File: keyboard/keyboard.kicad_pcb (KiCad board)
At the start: 4 copper layers, 83.3 x 34.3 mm, 23 parts, among them J1 Mini-DIN-6, J2 Conn_01x13, U1 74HC595, U2 74HC595, U3 74HC180, U4 74HC08, U5 74HC14

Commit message: Update keyboard
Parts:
- added C8: 1uF, Capacitor_THT:CP_Radial_D4.0mm_P2.00mm, F.Cu at (98.3, 62.9)
- H1, H2, H3, H4: footprint MountingHole:MountingHole_2.7mm_M2.5_Pad -> MountingHole:MountingHole_3.2mm_M3_Pad
- moved C2 2.29 mm to (89.9, 78.0)
- moved R3 1.93 mm to (90.1, 63.2)
- moved R2 1.80 mm to (89.9, 82.8)
- moved J1 1.50 mm to (82.3, 77.0), turned to 270 degrees
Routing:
- net VCC: track 146.6 -> 142.2 mm
- net KBD_DATA: track 28.9 -> 24.6 mm
- net KBD_CLK: track 87.1 -> 87.8 mm

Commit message: Update keyboard
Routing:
- added copper zone on F.Cu, net GND
- added copper zone on In1.Cu, net GND
- added copper zone on In2.Cu, net GND
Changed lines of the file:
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@@
     (pcbplotparams
       (layerselection 0x010fc_ffffffff)
-      (usegerberextensions false)
-      (usegerberattributes true)
-      (usegerberadvancedattributes true)
-      (creategerberjobfile true)
+      (usegerberextensions true)
+      (usegerberattributes false)
+      (usegerberadvancedattributes false)
+      (creategerberjobfile false)
       (excludeedgelayer true)
       (linewidth 0.100000)
@@
       (psa4output false)
       (plotreference true)
-      (plotvalue true)
+      (plotvalue false)
       (plotinvisibletext false)
       (padsonsilk false)
-      (subtractmaskfromsilk false)
+      (subtractmaskfromsilk true)
       (outputformat 1)
       (mirror false)
-      (drillshape 1)
+      (drillshape 0)
       (scaleselection 1)
-      (outputdirectory ""))
+      (outputdirectory "./gerbers"))
   )
   (net 0 "")
@@
       (effects (font (size 1 1) (thickness 0.15)))
     )
-    (fp_text user %R (at 0.3 0) (layer F.Fab)
-      (effects (font (size 1 1) (thickness 0.15)))
-    )
     (fp_circle (center 0 0) (end 3.2 0) (layer Cmts.User) (width 0.15))
     (fp_circle (center 0 0) (end 3.45 0) (layer F.CrtYd) (width 0.05))
+    (fp_text user %R (at 0.3 0) (layer F.Fab)
+      (effects (font (size 1 1) (thickness 0.15)))
+    )
     (pad 1 thru_hole circle (at 0 0) (size 6.4 6.4) (drill 3.2) (layers *.Cu *.Mask)
       (net 1 GND))
@@
       (effects (font (size 1 1) (thickness 0.15)))
     )
-    (fp_text user %R (at 0.3 0) (layer F.Fab)
-      (effects (font (size 1 1) (thickness 0.15)))
-    )
     (fp_circle (center 0 0) (end 3.2 0) (layer Cmts.User) (width 0.15))
     (fp_circle (center 0 0) (end 3.45 0) (layer F.CrtYd) (width 0.05))
+    (fp_text user %R (at 0.3 0) (layer F.Fab)
+      (effects (font (size 1 1) (thickness 0.15)))
+    )
     (pad 1 thru_hole circle (at 0 0) (size 6.4 6.4) (drill 3.2) (layers *.Cu *.Mask)
       (net 1 GND))
@@
       (effects (font (size 1 1) (thickness 0.15)))
     )
-    (fp_text user %R (at 0.3 0) (layer F.Fab)
-      (effects (font (size 1 1) (thickness 0.15)))
-    )
     (fp_circle (center 0 0) (end 3.2 0) (layer Cmts.User) (width 0.15))
     (fp_circle (center 0 0) (end 3.45 0) (layer F.CrtYd) (width 0.05))
+    (fp_text user %R (at 0.3 0) (layer F.Fab)
+      (effects (font (size 1 1) (thickness 0.15)))
+    )
     (pad 1 thru_hole circle (at 0 0) (size 6.4 6.4) (drill 3.2) (layers *.Cu *.Mask)
       (net 1 GND))
@@
       (effects (font (size 1 1) (thickness 0.15)))
     )
-    (fp_text user %R (at 0.3 0) (layer F.Fab)
-      (effects (font (size 1 1) (thickness 0.15)))
-    )
     (fp_circle (center 0 0) (end 3.2 0) (layer Cmts.User) (width 0.15))
     (fp_circle (center 0 0) (end 3.45 0) (layer F.CrtYd) (width 0.05))
+    (fp_text user %R (at 0.3 0) (layer F.Fab)
+      (effects (font (size 1 1) (thickness 0.15)))
+    )
     (pad 1 thru_hole circle (at 0 0) (size 6.4 6.4) (drill 3.2) (layers *.Cu *.Mask)
       (net 1 GND))
@@
       )
     )
+  )
+  (zone (net 1) (net_name GND) (layer F.Cu) (hatch edge 0.508)
+    (connect_pads (clearance 0.508))
+    (min_thickness 0.254)
+    (fill yes (arc_segments 32) (thermal_gap 0.508) (thermal_bridge_width 0.508))
+    (polygon
+      (pts
+        (xy 161.036 97.536) (xy 73.533 97.028) (xy 73.152 57.404) (xy 161.036 57.15)
+      )
+    )
+  )
+  (zone (net 1) (net_name GND) (layer In1.Cu) (hatch edge 0.508)
+    (connect_pads (clearance 0.508))
+    (min_thickness 0.254)
+    (fill yes (arc_segments 32) (thermal_gap 0.508) (thermal_bridge_width 0.508))
+    (polygon
+      (pts
+        (xy 161.29 97.536) (xy 73.406 96.901) (xy 73.406 57.531) (xy 161.29 57.15)
+      )
+    )
+  )
+  (zone (net 1) (net_name GND) (layer In2.Cu) (hatch edge 0.508)
+    (connect_pads (clearance 0.508))
+    (min_thickness 0.254)
+    (fill yes (arc_segments 32) (thermal_gap 0.508) (thermal_bridge_width 0.508))
+    (polygon
+      (pts
+        (xy 161.163 57.531) (xy 161.29 97.536) (xy 73.406 97.028) (xy 73.406 57.404)
+      )
+    )

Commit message: Update keyboard PCB
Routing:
- net KBD_CLK: track 87.8 -> 80.4 mm
- net VCC: track 142.2 -> 143.1 mm
- net KBD_DATA: track 24.6 -> 23.9 mm
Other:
- board text added: "PS/2 interface v1.1 Adrien Kohlbecker 2021-05-18"
- board text removed: "PS/2 interface v01 Adrien Kohlbecker 2021-05-18"
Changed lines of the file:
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@@
     (thickness 1.6)
     (drawings 27)
-    (tracks 261)
+    (tracks 260)
     (zones 0)
     (modules 24)
@@
     (add_net ~REG_CLK)
     (add_net ~REG_OE)
+  )
+  (module AK's_Footprints:Mini_din6 (layer F.Cu)
+    (at 82.2706 76.962 270)
+    (tags "MINI DIN")
+    (fp_text reference J1 (at 0 -7.62 270) (layer F.Fab)
+      (effects (font (size 1.524 1.524) (thickness 0.3048)))
+    )
+    (fp_text value Mini-DIN-6 (at 0 -10.16 90) (layer F.Fab)
+      (effects (font (size 1.524 1.524) (thickness 0.3048)))
+    )
+    (fp_line (start -6.35 1.27) (end -6.35 -5.68) (layer F.SilkS) (width 0.1))
+    (fp_line (start -6.35 -5.68) (end 6.35 -5.68) (layer F.SilkS) (width 0.1))
+    (fp_line (start 6.35 -5.68) (end 6.35 6.58) (layer F.SilkS) (width 0.1))
+    (fp_line (start 6.35 6.58) (end -6.35 6.58) (layer F.SilkS) (width 0.1))
+    (fp_line (start -6.35 6.58) (end -6.35 1.27) (layer F.SilkS) (width 0.1))
+    (pad GND thru_hole rect (at -6.985 1.27 270) (size 2.16916 3.2004) (drill oval 0.5 1.9) (layers *.Cu *.Mask)
+      (net 1 GND))
+    (pad GND thru_hole rect (at 6.985 1.27 270) (size 2.16916 3.2004) (drill oval 0.5 1.9) (layers *.Cu *.Mask)
+      (net 1 GND))
+    (pad GND thru_hole rect (at 0 1.8542 270) (size 3.2004 1.99898) (drill oval 1.9 0.5) (layers *.Cu *.Mask)
+      (net 1 GND))
+    (pad 3 thru_hole circle (at 3.175 -1.27 270) (size 1.7 1.7) (drill 0.75) (layers *.Cu *.Mask)
+      (net 1 GND))
+    (pad 4 thru_hole circle (at -3.175 -1.27 270) (size 1.7 1.7) (drill 0.75) (layers *.Cu *.Mask)
+      (net 3 VCC))
+    (pad 6 thru_hole circle (at -3.175 -3.81 270) (size 1.7 1.7) (drill 0.75) (layers *.Cu *.Mask))
+    (pad 5 thru_hole circle (at 3.175 -3.81 270) (size 1.7 1.7) (drill 0.75) (layers *.Cu *.Mask)
+      (net 16 KBD_CLK))
+    (pad 1 thru_hole circle (at 1.143 -1.27 270) (size 1.7 1.7) (drill 0.75) (layers *.Cu *.Mask)
+      (net 17 KBD_DATA))
+    (pad 2 thru_hole circle (at -1.016 -1.27 270) (size 1.7 1.7) (drill 0.75) (layers *.Cu *.Mask))
+    (model ":AKs Footprints:Mini_din6.wrl"
+      (at (xyz 0 0 0))
+      (scale (xyz 1 1 1))
+      (rotate (xyz 0 0 0))
+    )
   )
   (module MountingHole:MountingHole_3.2mm_M3_Pad (layer F.Cu)
@@
     )
   )
-  (module AK's_Footprints:Mini_din6 (layer F.Cu)
-    (at 82.2706 76.962 270)
-    (tags "MINI DIN")
-    (fp_text reference J1 (at 0 -7.62 270) (layer F.Fab)
-      (effects (font (size 1.524 1.524) (thickness 0.3048)))
-    )
-    (fp_text value Mini-DIN-6 (at 0 -10.16 90) (layer F.Fab)
-      (effects (font (size 1.524 1.524) (thickness 0.3048)))
-    )
-    (fp_line (start -6.35 1.27) (end -6.35 -5.68) (layer F.SilkS) (width 0.1))
-    (fp_line (start -6.35 -5.68) (end 6.35 -5.68) (layer F.SilkS) (width 0.1))
-    (fp_line (start 6.35 -5.68) (end 6.35 6.58) (layer F.SilkS) (width 0.1))
-    (fp_line (start 6.35 6.58) (end -6.35 6.58) (layer F.SilkS) (width 0.1))
-    (fp_line (start -6.35 6.58) (end -6.35 1.27) (layer F.SilkS) (width 0.1))
-    (pad GND thru_hole rect (at -6.985 1.27 270) (size 2.16916 3.2004) (drill oval 0.5 1.9) (layers *.Cu *.Mask)
-      (net 1 GND))
-    (pad GND thru_hole rect (at 6.985 1.27 270) (size 2.16916 3.2004) (drill oval 0.5 1.9) (layers *.Cu *.Mask)
-      (net 1 GND))
-    (pad GND thru_hole rect (at 0 1.8542 270) (size 3.2004 1.99898) (drill oval 1.9 0.5) (layers *.Cu *.Mask)
-      (net 1 GND))
-    (pad 2 thru_hole circle (at 3.175 -1.27 270) (size 1.7 1.7) (drill 0.75) (layers *.Cu *.Mask))
-    (pad 5 thru_hole circle (at -3.175 -1.27 270) (size 1.7 1.7) (drill 0.75) (layers *.Cu *.Mask)
-      (net 16 KBD_CLK))
-    (pad 6 thru_hole circle (at -3.175 -3.81 270) (size 1.7 1.7) (drill 0.75) (layers *.Cu *.Mask))
-    (pad 1 thru_hole circle (at 3.175 -3.81 270) (size 1.7 1.7) (drill 0.75) (layers *.Cu *.Mask)
-      (net 17 KBD_DATA))
-    (pad 3 thru_hole circle (at 1.143 -1.27 270) (size 1.7 1.7) (drill 0.75) (layers *.Cu *.Mask)
-      (net 1 GND))
-    (pad 4 thru_hole circle (at -1.016 -1.27 270) (size 1.7 1.7) (drill 0.75) (layers *.Cu *.Mask)
-      (net 3 VCC))
-    (model ":AKs Footprints:Mini_din6.wrl"
-      (at (xyz 0 0 0))
-      (scale (xyz 1 1 1))
-      (rotate (xyz 0 0 0))
-    )
-  )
   (module Package_DIP:DIP-14_W7.62mm (layer F.Cu)
     (at 136.906 72.898)
@@
     )
   )
-  (gr_text "PS/2 interface v01\nAdrien Kohlbecker\n2021-05-18" (at 91.186 66.802) (layer B.SilkS)
+  (gr_text "PS/2 interface v1.1\nAdrien Kohlbecker\n2021-05-18" (at 91.186 66.802) (layer B.SilkS)
     (effects (font (size 1 1) (thickness 0.15)) (justify mirror))
   )
@@
     (effects (font (size 1 1) (thickness 0.15)))
   )
-  (gr_text 74HC14 (at 139.192 75.438 90) (layer F.SilkS)
-    (effects (font (size 1 1) (thickness 0.15)))
-  )
-  (gr_text 74HC08 (at 128.27 75.438 90) (layer F.SilkS)
-    (effects (font (size 1 1) (thickness 0.15)))
-  )
-  (gr_text 74HC180 (at 117.348 75.692 90) (layer F.SilkS)
-    (effects (font (size 1 1) (thickness 0.15)))
-  )
-  (gr_text 74HC595 (at 106.426 75.692 90) (layer F.SilkS)
-    (effects (font (size 1 1) (thickness 0.15)))
-  )
-  (gr_text 74HC595 (at 95.504 75.692 90) (layer F.SilkS)
+  (gr_text 74HC14 (at 140.8176 77.6732 90) (layer F.SilkS)
+    (effects (font (size 1 1) (thickness 0.15)))
+  )
+  (gr_text 74HC08 (at 129.921 77.7748 90) (layer F.SilkS)
+    (effects (font (size 1 1) (thickness 0.15)))
+  )
+  (gr_text 74HC180 (at 118.9228 77.8256 90) (layer F.SilkS)
+    (effects (font (size 1 1) (thickness 0.15)))
+  )
+  (gr_text 74HC595 (at 108.077 78.0542 90) (layer F.SilkS)
+    (effects (font (size 1 1) (thickness 0.15)))
+  )
+  (gr_text 74HC595 (at 97.2312 78.232 90) (layer F.SilkS)
     (effects (font (size 1 1) (thickness 0.15)))
   )
@@
   (segment (start 94.996 66.548) (end 90.678 66.548) (width 0.762) (layer B.Cu) (net 3))
   (segment (start 87.2744 75.946) (end 89.3318 78.0034) (width 0.762) (layer B.Cu) (net 3))
-  (segment (start 83.5406 75.946) (end 87.2744 75.946) (width 0.762) (layer B.Cu) (net 3))
   (segment (start 89.3318 82.2198) (end 89.9414 82.8294) (width 0.762) (layer B.Cu) (net 3))
   (segment (start 89.3318 78.0034) (end 89.3318 82.2198) (width 0.762) (layer B.Cu) (net 3))
@@
   (segment (start 98.298 66.294) (end 98.552 66.548) (width 0.762) (layer B.Cu) (net 3))
   (segment (start 98.298 62.865) (end 98.298 66.294) (width 0.762) (layer B.Cu) (net 3))
+  (segment (start 85.6996 75.946) (end 83.5406 73.787) (width 0.762) (layer B.Cu) (net 3))
+  (segment (start 87.2744 75.946) (end 85.6996 75.946) (width 0.762) (layer B.Cu) (net 3))
   (segment (start 148.844 76.708) (end 148.844 81.28) (width 0.254) (layer F.Cu) (net 4))
   (segment (start 145.938999 84.185001) (end 148.844 81.28) (width 0.254) (layer F.Cu) (net 4))
@@
   (segment (start 133.746999 91.805001) (end 90.789001 91.805001) (width 0.254) (layer F.Cu) (net 16))
   (segment (start 134.874 90.678) (end 133.746999 91.805001) (width 0.254) (layer F.Cu) (net 16))
-  (segment (start 84.717601 85.225601) (end 89.9414 90.4494) (width 0.254) (layer F.Cu) (net 16))
-  (segment (start 84.717601 74.964001) (end 84.717601 85.225601) (width 0.254) (layer F.Cu) (net 16))
-  (segment (start 83.5406 73.787) (end 84.717601 74.964001) (width 0.254) (layer F.Cu) (net 16))
   (segment (start 90.789001 91.297001) (end 90.789001 91.805001) (width 0.254) (layer F.Cu) (net 16))
   (segment (start 89.9414 90.4494) (end 90.789001 91.297001) (width 0.254) (layer F.Cu) (net 16))
-  (segment (start 86.0806 75.85817) (end 86.0806 80.137) (width 0.254) (layer F.Cu) (net 17))
-  (segment (start 89.9414 71.99737) (end 86.0806 75.85817) (width 0.254) (layer F.Cu) (net 17))
+  (segment (start 86.0806 86.5886) (end 86.0806 80.137) (width 0.25) (layer F.Cu) (net 16))
+  (segment (start 89.9414 90.4494) (end 86.0806 86.5886) (width 0.25) (layer F.Cu) (net 16))
   (segment (start 93.726 70.866) (end 90.0684 70.866) (width 0.254) (layer F.Cu) (net 17))
   (segment (start 100.838 77.978) (end 93.726 70.866) (width 0.254) (layer F.Cu) (net 17))
-  (segment (start 89.9414 70.993) (end 90.0684 70.866) (width 0.254) (layer F.Cu) (net 17))
-  (segment (start 89.9414 71.99737) (end 89.9414 70.993) (width 0.254) (layer F.Cu) (net 17))
+  (segment (start 83.96077 78.105) (end 83.5406 78.105) (width 0.25) (layer F.Cu) (net 17))
+  (segment (start 90.0684 71.99737) (end 83.96077 78.105) (width 0.25) (layer F.Cu) (net 17))
+  (segment (start 90.0684 70.866) (end 90.0684 71.99737) (width 0.25) (layer F.Cu) (net 17))
   (segment (start 108.965037 76.565001) (end 111.260438 74.2696) (width 0.254) (layer In2.Cu) (net 18))
   (segment (start 100.838 75.438) (end 101.965001 76.565001) (width 0.254) (layer In2.Cu) (net 18))

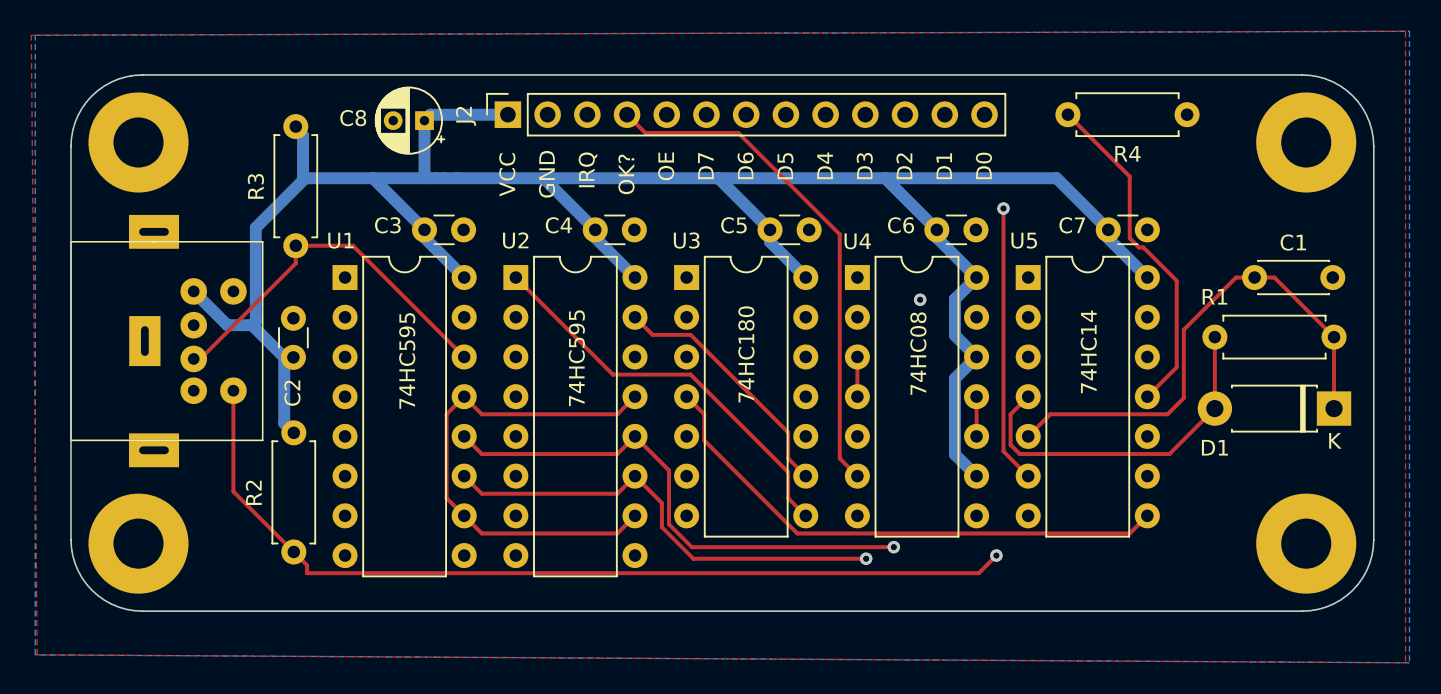
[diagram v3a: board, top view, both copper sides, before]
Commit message: Updated keyboard
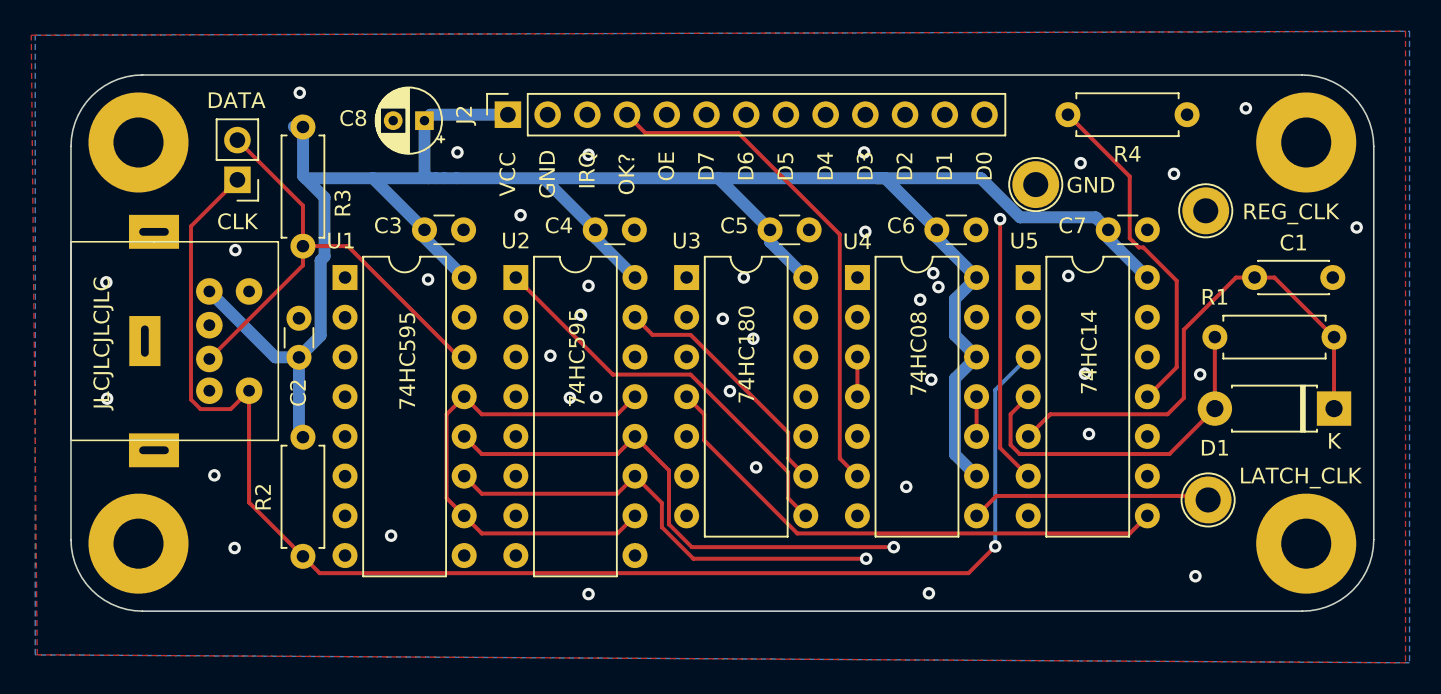
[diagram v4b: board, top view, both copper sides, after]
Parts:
- added J3: KBD, Connector_PinHeader_2.54mm:PinHeader_1x02_P2.54mm_Vertical, F.Cu at (86.3, 66.6)
- added TP1: REG_CLK, TestPoint:TestPoint_Loop_D2.60mm_Drill1.6mm_Beaded, F.Cu at (148.3, 68.6)
- added TP2: LATCH_CLK, TestPoint:TestPoint_Loop_D2.60mm_Drill1.6mm_Beaded, F.Cu at (148.4, 87.1)
- added TP3: GND, TestPoint:TestPoint_Loop_D2.60mm_Drill1.6mm_Beaded, F.Cu at (137.4, 67.0)
- C8: value 1uF -> 10uF
- J1: footprint AK's_Footprints:Mini_din6 -> AK's_Footprints:PS2_mini_din_6
- moved R2 0.65 mm to (90.5, 83.1)
- moved R3 0.46 mm to (90.5, 63.3)
- moved C2 0.36 mm to (90.3, 78.0)
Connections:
- J1 pad 2: (no net) -> Net-(J1-Pad2)
- J1 pad 6: (no net) -> Net-(J1-Pad6)
- U2 pad 3: (no net) -> Net-(U2-Pad3)
- U2 pad 4: (no net) -> Net-(U2-Pad4)
- U2 pad 5: (no net) -> Net-(U2-Pad5)
- U2 pad 6: (no net) -> Net-(U2-Pad6)
- U2 pad 7: (no net) -> Net-(U2-Pad7)
- U2 pad 9: (no net) -> Net-(U2-Pad9)
- U3 pad 6: (no net) -> Net-(U3-Pad6)
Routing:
- net KBD_CLK: track 80.4 -> 99.2 mm
- net ~LATCH_CLK: track 39.5 -> 54.9 mm
- net ~REG_CLK: track 60.1 -> 70.6 mm
- net KBD_DATA: track 23.9 -> 31.5 mm
- net VCC: track 143.1 -> 145.5 mm
- net IRQ: track 46.9 -> 46.3 mm
- net GND: vias 0 -> 38
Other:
- board text added: "CLK"
- board text added: "DATA"
- board text added: "JLCJLCJLCJLC"
